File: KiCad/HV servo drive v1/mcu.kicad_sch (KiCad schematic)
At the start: 26 parts, among them J3 PROG, U22 PL133-37TC, U5 STM32F413RGT6, U9 AP2127K-3.3

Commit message: KiCad 8.0 update
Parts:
- renumbered C89 to C12, C12 to C14, C14 to C15, C38 to C17, C15 to C20, C17 to C21, C25 to C22, C20 to C24, C21 to C25, C41 to C38, C22 to C41, C24 to C89, R18 to R10, R19 to R18, R20 to R19, R21 to R20, R22 to R21, R23 to R22, R10 to R23, TP1 to TP21, TP1 to TP22, U9 to U22, U22 to U5, U5 to U9

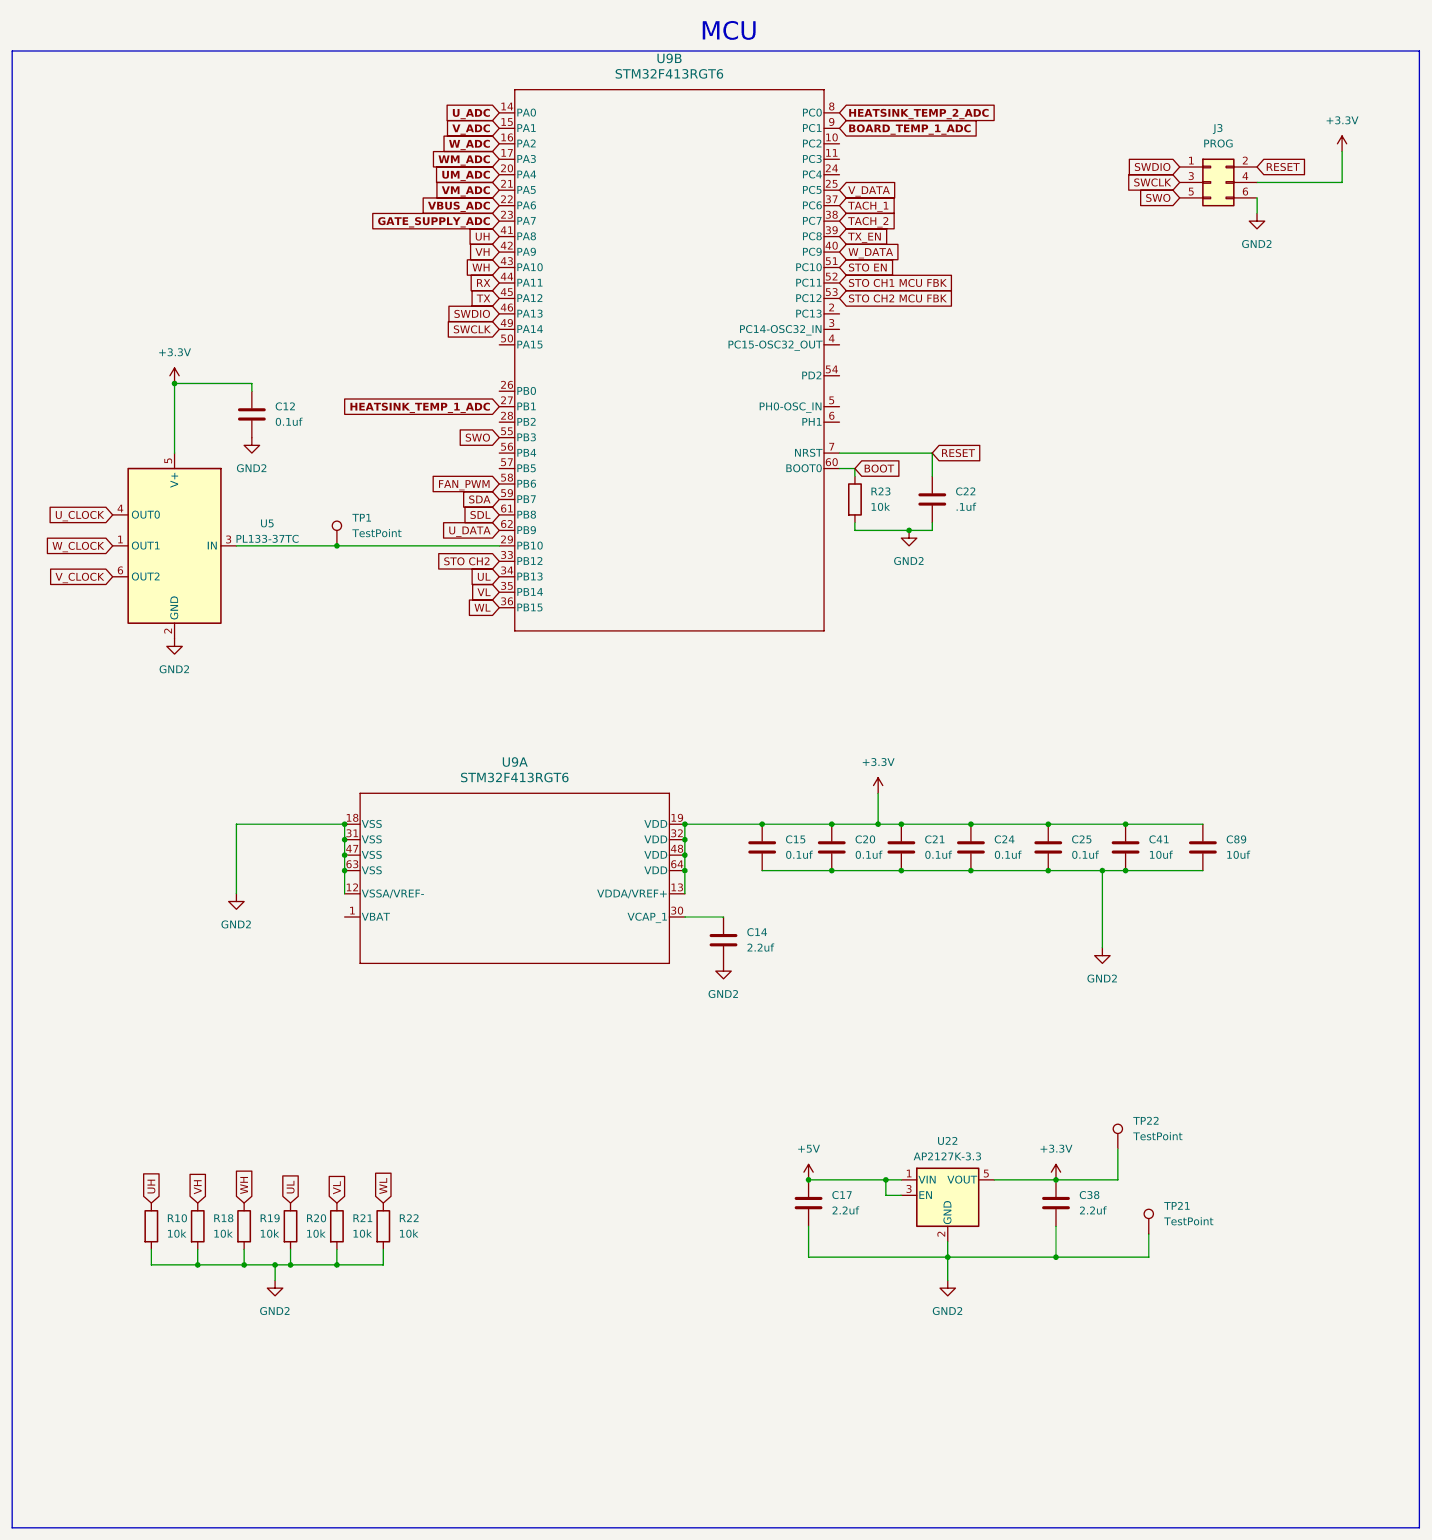
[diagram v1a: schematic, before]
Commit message: start rev 2 changes
fix component references, fix rj45 and dc-dc converter footprints, add RLC filters on all power connectors, add more mounting holes
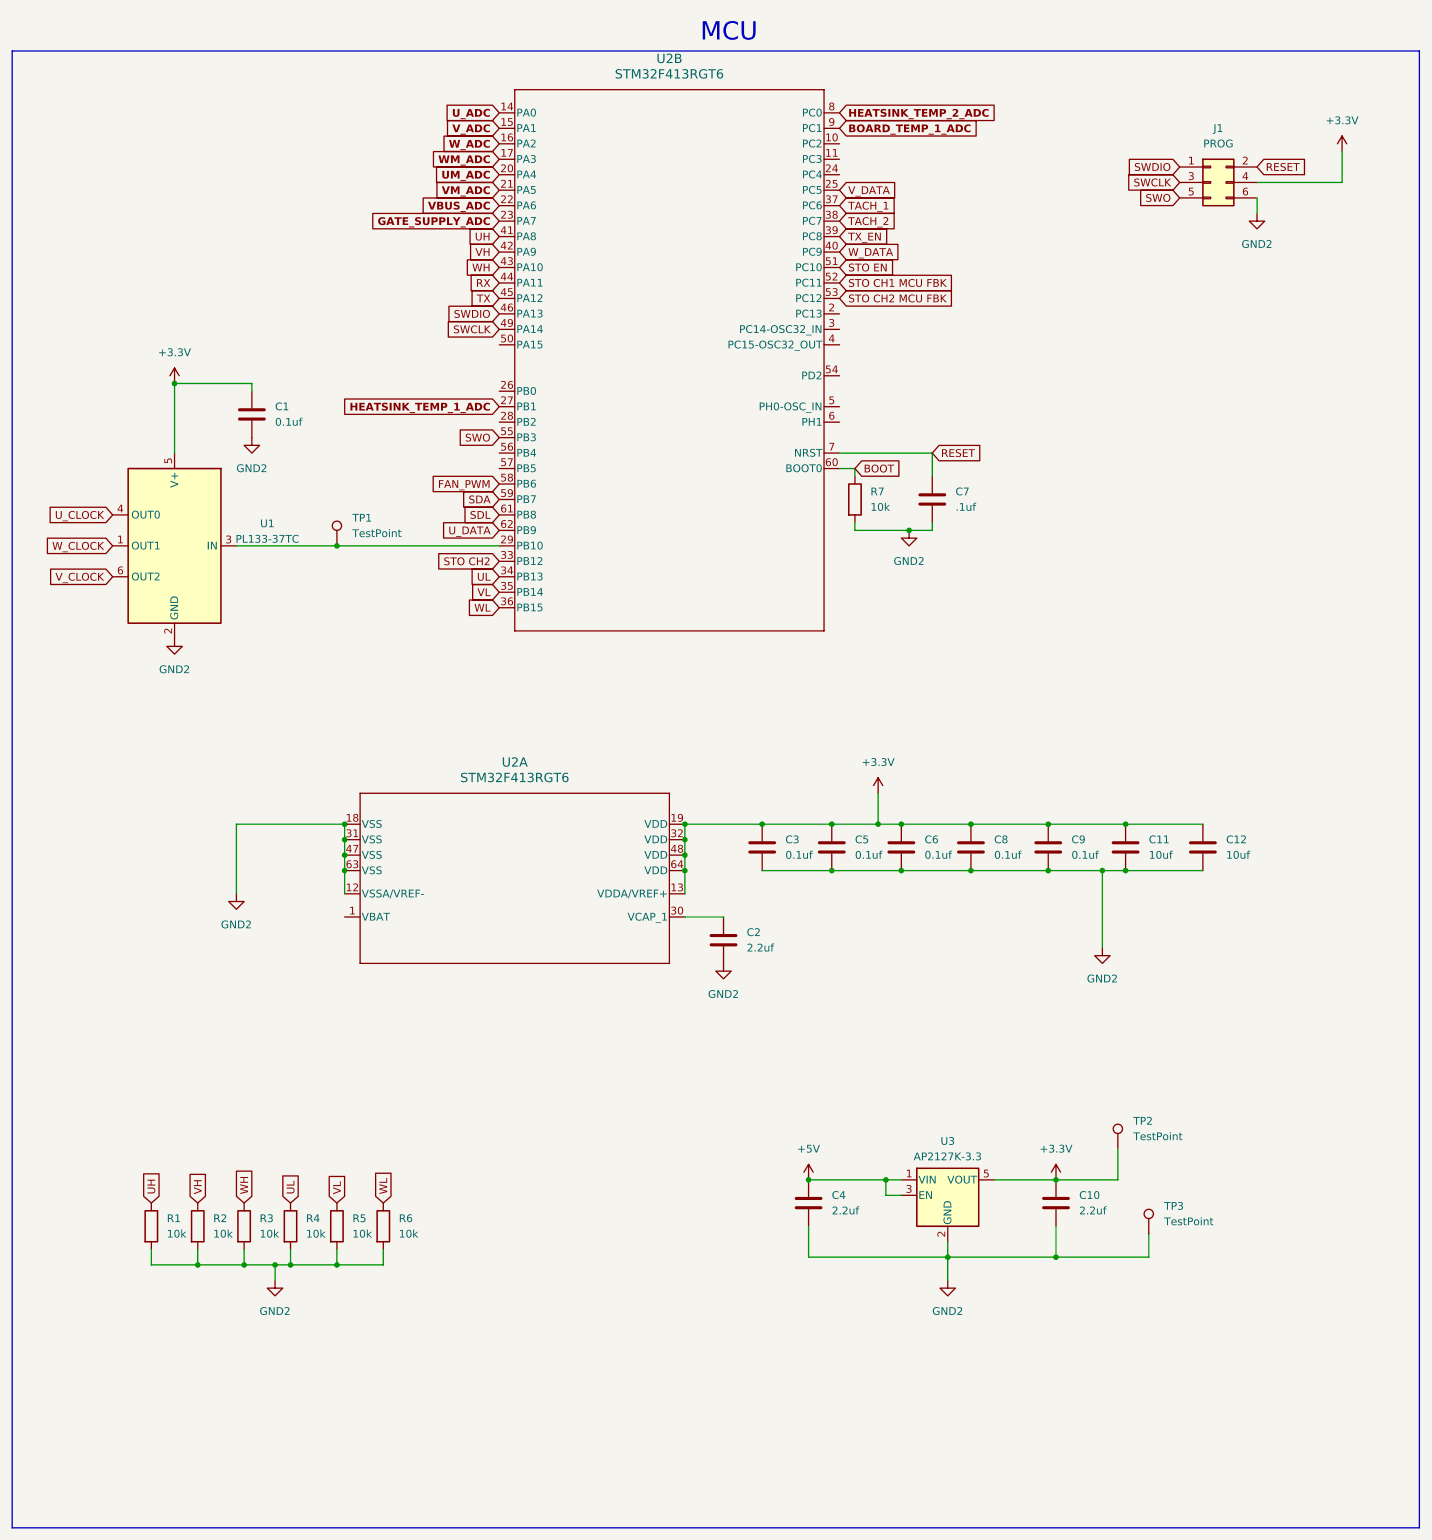
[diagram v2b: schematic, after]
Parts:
- renumbered C12 to C1, C38 to C10, C41 to C11, C89 to C12, C14 to C2, C15 to C3, C17 to C4, C20 to C5, C21 to C6, C22 to C7, C24 to C8, C25 to C9, J3 to J1, R10 to R1, R18 to R2, R19 to R3, R20 to R4, R21 to R5, R22 to R6, R23 to R7, TP22 to TP2, TP21 to TP3, U5 to U1, U9 to U2, U22 to U3

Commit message: update to rev 2.1
basically the same version as in the FOC youtube video, with some minor issues fixed
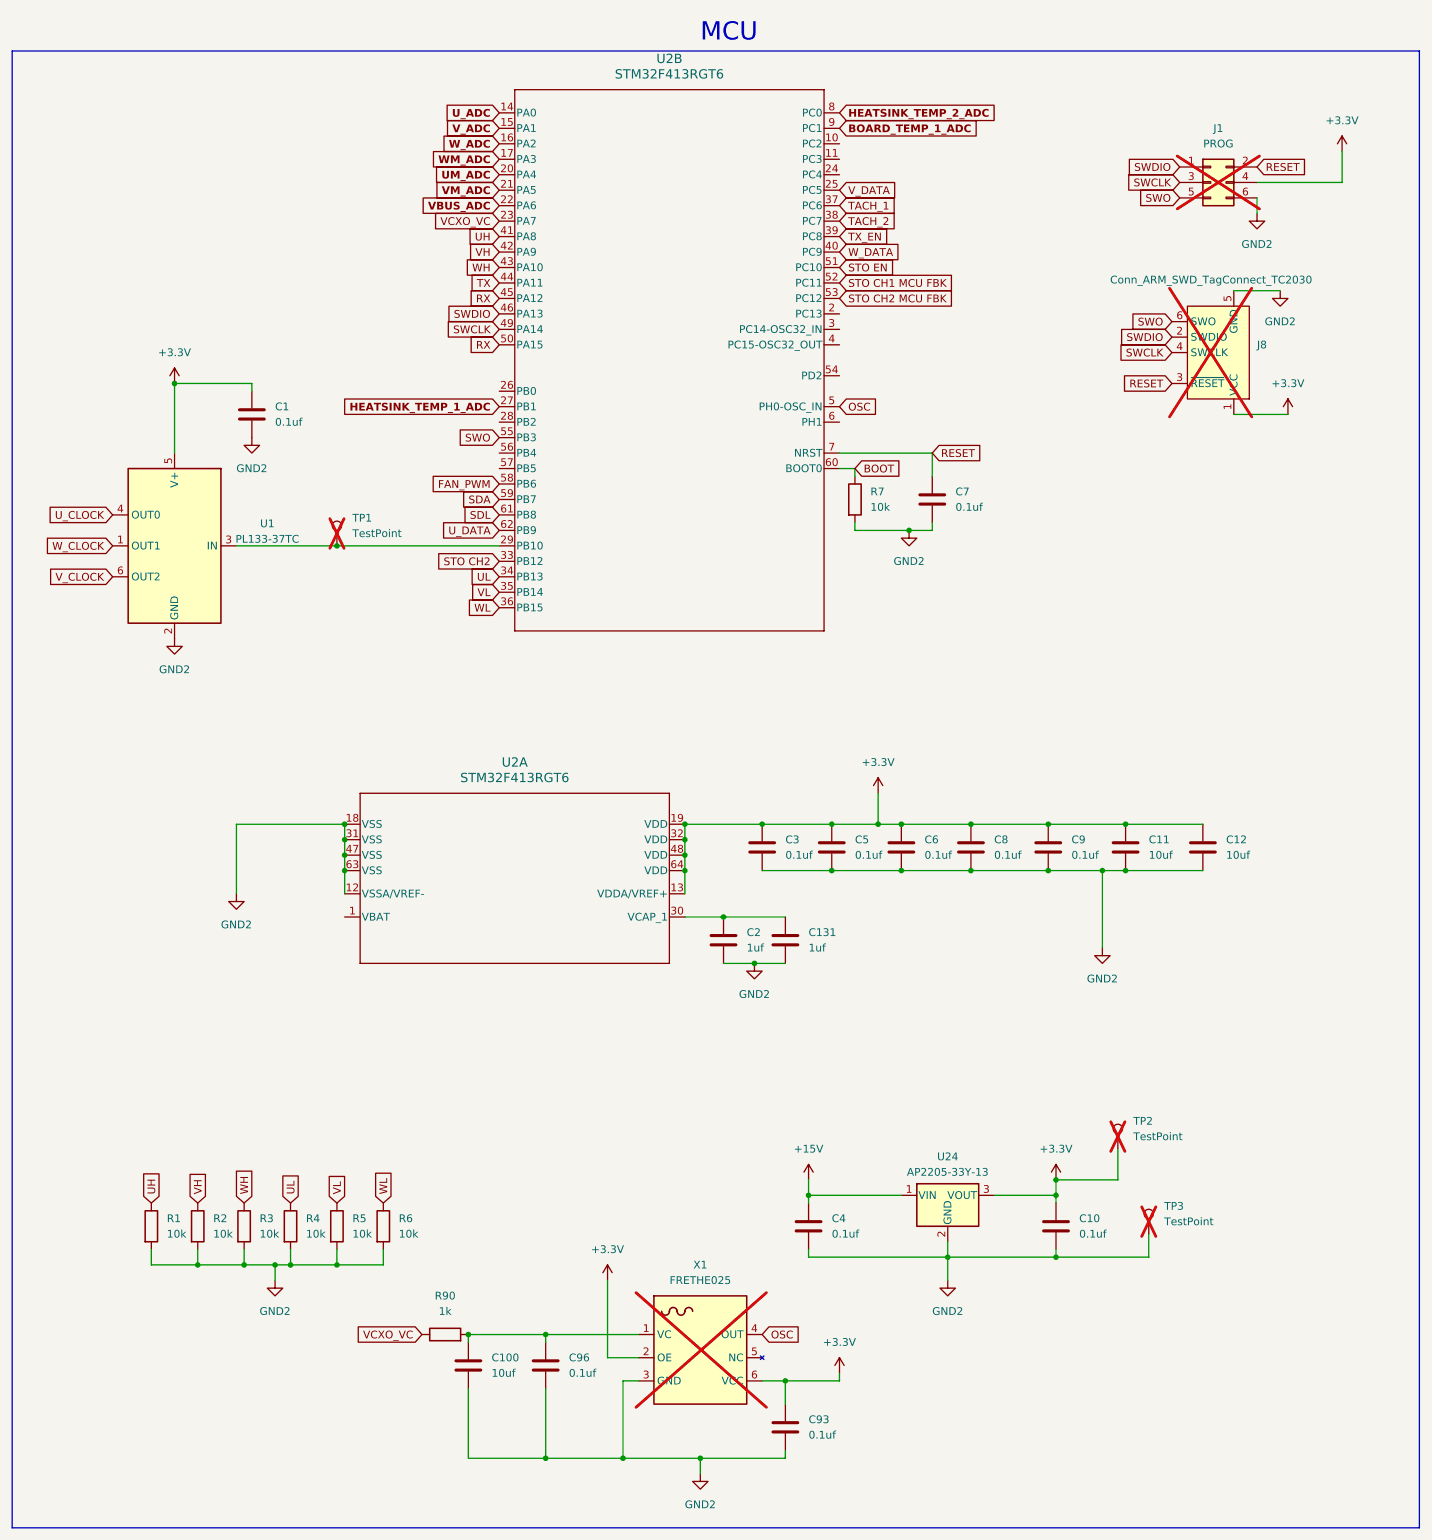
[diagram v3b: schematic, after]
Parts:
- removed U3: AP2127K-3.3, Package_TO_SOT_SMD:SOT-23-5, symbol Regulator_Linear:AP2127K-3.3
- added C100: 10uf, Capacitor_SMD:C_0805_2012Metric, symbol Device:C
- added C131: 1uf, Capacitor_SMD:C_0603_1608Metric, symbol Device:C
- added C93, C96: 0.1uf, Capacitor_SMD:C_0603_1608Metric, symbol Device:C
- added J8: Conn_ARM_SWD_TagConnect_TC2030, Connector:Tag-Connect_TC2030-IDC-FP_2x03_P1.27mm_Vertical, symbol Connector:Conn_ARM_SWD_TagConnect_TC2030
- added R90: 1k, Resistor_SMD:R_0603_1608Metric, symbol Device:R
- added U24: AP2205-33Y-13, Package_TO_SOT_SMD:SOT-89-3, symbol Regulator_Linear:AP2204R-3.3
- added X1: FRETHE025, footprints:FR_3-3V, symbol FR_3-3V:FRETHE025
- C1, C3, C5, C6, C8, C9: Generic Allowed? (none) -> yes; Manufacturer (none) -> YAGEO; Part number (none) -> CC0603ZRY5V9BB104
- C10, C4: value 2.2uf -> 0.1uf; Generic Allowed? (none) -> yes; Manufacturer (none) -> YAGEO; Part number (none) -> CC0603ZRY5V9BB104
- C11, C12: Generic Allowed? (none) -> yes; Manufacturer (none) -> Murata Electronics; Part number (none) -> GRM21BR61H106KE43L
- C2: value 2.2uf -> 1uf; Generic Allowed? (none) -> yes; Manufacturer (none) -> Samsung Electro-Mechanics; Part number (none) -> CL10A105KB8NNNC
- C7: value .1uf -> 0.1uf; Generic Allowed? (none) -> yes; Manufacturer (none) -> YAGEO; Part number (none) -> CC0603ZRY5V9BB104
- J1, TP1, TP2, TP3: now not fitted
- R1, R2, R3, R4, R5, R6, R7: Generic Allowed? (none) -> yes; Manufacturer (none) -> YAGEO; Part number (none) -> RC0603FR-0710KL
- U1: Generic Allowed? (none) -> yes; Manufacturer (none) -> Microchip Technology; Part number (none) -> PL133-37TC
- U2: Generic Allowed? (none) -> no; Manufacturer (none) -> STMicroelectronics; Part number (none) -> STM32F413RGT6
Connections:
- net +3.3V: now also C93.1, J8.1 (VCC), U24.3 (VOUT), X1.2 (OE), X1.6 (VCC)
- net GND2: now also C100.2, C131.2, C93.2, C96.2, J8.5 (GND), U24.2 (GND), X1.3 (GND)
- net RESET: now also J8.3 (~{RESET})
- net RX: now also U2.45 (PA12), U2.50 (PA15); no longer U2.44 (PA11)
- net SWCLK: now also J8.4 (SWCLK)
- net SWDIO: now also J8.2 (SWDIO)
- net SWO: now also J8.6 (SWO)
- net TX: now also U2.44 (PA11); no longer U2.45 (PA12)
- net at C2.1, U2.30 (VCAP_1): now also C131.1
- net OSC: now reaches U2.5 (PH0-OSC_IN)
- net OSC: now also X1.4 (OUT)
- net +5V renamed +15V
- net +15V: now also U24.1 (VIN)
- net GATE_SUPPLY_ADC renamed VCXO_VC
- net VCXO_VC: now also R90.1
- new net: C100.1, C96.1, R90.2, X1.1 (VC)
